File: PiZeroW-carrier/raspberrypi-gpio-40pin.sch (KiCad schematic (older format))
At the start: 8 parts, among them J1 40HAT, J2 CONN_02X02

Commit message: fix symbol for socket strip
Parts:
- removed J1: 40HAT, Socket_Strips:Socket_Strip_Straight_2x20, symbol OX40HAT
- added P?: CONN_02X20, Socket_Strips:Socket_Strip_Straight_2x20, symbol CONN_02X20
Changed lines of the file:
@@
 F 2 "project_footprints:NPTH_3mm_ID" H 5550 6000 60  0001 C CNN
 F 3 "" H 5550 6000 60  0001 C CNN
-F 4 "" H -12600 -4650 50  0001 C CNN "MFR"
-F 5 "" H -12600 -4650 50  0001 C CNN "MPN"
-F 6 "" H -12600 -4650 50  0001 C CNN "SPR"
-F 7 "" H -12600 -4650 50  0001 C CNN "SPN"
-F 8 "" H -12600 -4650 50  0001 C CNN "SPURL"
 	1    5650 6000
 	1    0    0    -1
@@
 F 8 "" H -12600 -4650 50  0001 C CNN "SPURL"
 	1    6700 6550
-	1    0    0    -1
-$EndComp
-$Comp
-L OX40HAT J1
-U 1 1 5A256561
-P 2600 2250
-F 0 "J1" H 2950 2350 50  0000 C CNN
-F 1 "40HAT" H 2300 2350 50  0000 C CNN
-F 2 "Socket_Strips:Socket_Strip_Straight_2x20" H 2600 2450 50  0000 C CNN
-F 3 "" H 1900 2250 50  0000 C CNN
-	1    2600 2250
 	1    0    0    -1
 $EndComp
@@
 Text Notes 5300 5700 0    118  ~ 24
 Mounting Holes
-Text Notes 1650 2000 0    118  ~ 24
+Text Notes 1600 1975 0    118  ~ 24
 40-Pin HAT Connector
-Text Label 800  4150 0    60   ~ 0
-GND
-Wire Wire Line
-	2000 4150 800  4150
-Text Label 800  3550 0    60   ~ 0
+Text Label 1150 4150 0    60   ~ 0
+GND
+Wire Wire Line
+	2350 4150 1150 4150
+Text Label 1150 3550 0    60   ~ 0
 SDA
 Wire Wire Line
-	2000 3550 800  3550
-Text Label 800  3450 0    60   ~ 0
-GND
-Wire Wire Line
-	2000 3450 800  3450
-Text Label 800  2650 0    60   ~ 0
-GND
-Wire Wire Line
-	2000 2650 800  2650
-Text Label 800  2250 0    60   ~ 0
+	2350 3550 1150 3550
+Text Label 1150 3450 0    60   ~ 0
+GND
+Wire Wire Line
+	2350 3450 1150 3450
+Text Label 1150 2650 0    60   ~ 0
+GND
+Wire Wire Line
+	2350 2650 1150 2650
+Text Label 1150 2250 0    60   ~ 0
 P3V3_HAT
 Wire Wire Line
-	2000 2250 800  2250
-Wire Wire Line
-	3200 2850 4400 2850
-Wire Wire Line
-	3200 3150 4400 3150
-Wire Wire Line
-	3200 3550 4400 3550
-Wire Wire Line
-	3200 3650 4400 3650
-Wire Wire Line
-	3200 3850 4400 3850
-Text Label 4400 2850 2    60   ~ 0
-GND
-Text Label 4400 3150 2    60   ~ 0
-GND
-Text Label 4400 3650 2    60   ~ 0
-GND
-Text Label 4400 3550 2    60   ~ 0
+	2350 2250 1150 2250
+Wire Wire Line
+	2850 2850 4050 2850
+Wire Wire Line
+	2850 3150 4050 3150
+Wire Wire Line
+	2850 3550 4050 3550
+Wire Wire Line
+	2850 3650 4050 3650
+Wire Wire Line
+	2850 3850 4050 3850
+Text Label 4050 2850 2    60   ~ 0
+GND
+Text Label 4050 3150 2    60   ~ 0
+GND
+Text Label 4050 3650 2    60   ~ 0
+GND
+Text Label 4050 3550 2    60   ~ 0
 SCL
-Text Label 4400 3850 2    60   ~ 0
-GND
-Text Label 4400 2450 2    60   ~ 0
-GND
-Wire Wire Line
-	3200 2450 4400 2450
-Wire Wire Line
-	3200 2350 4400 2350
-Wire Wire Line
-	3200 2250 4400 2250
+Text Label 4050 3850 2    60   ~ 0
+GND
+Text Label 4050 2450 2    60   ~ 0
+GND
+Wire Wire Line
+	2850 2450 4050 2450
+Wire Wire Line
+	2850 2350 4050 2350
+Wire Wire Line
+	2850 2250 4050 2250
 Text Notes 7150 4950 0    60   ~ 0
 HAT spec indicates to NEVER\npower the 3.3V pins on the Raspberry Pi \nfrom the HAT header. Only connect the 3.3V\npower from the Pi if the HAT does not have\n3.3V on board.\n\nIF you are designing a board that could\neither be powered by the Pi or from the HAT\nthe jumpers here can be used.\n\nIn most cases, either design the HAT \nto provide the 5V to the Pi and use the\nprotection circuit above OR power the\nHAT from the Pi and directly connect\nthe P3V3 and P5V to the P3V3_HAT and P5V_HAT\npins.
@@
 Text HLabel 5250 4700 0    60   Input ~ 0
 +5V
-Text HLabel 1145 2750 0    60   Input ~ 0
+Text HLabel 1495 2750 0    60   Input ~ 0
 LEDEnable
 Wire Wire Line
-	1145 2750 2000 2750
-NoConn ~ 2000 2350
-NoConn ~ 2000 2450
-NoConn ~ 2000 2550
-NoConn ~ 2000 2950
-NoConn ~ 2000 3050
-NoConn ~ 2000 3150
-NoConn ~ 2000 3250
-NoConn ~ 2000 3350
-NoConn ~ 2000 3650
-NoConn ~ 2000 3750
-NoConn ~ 2000 3850
-NoConn ~ 2000 3950
-NoConn ~ 2000 4050
-NoConn ~ 3200 4150
-NoConn ~ 3200 4050
-NoConn ~ 3200 3950
-NoConn ~ 3200 3750
-NoConn ~ 3200 3450
-NoConn ~ 3200 3350
-NoConn ~ 3200 3250
-NoConn ~ 3200 3050
-NoConn ~ 3200 2950
-NoConn ~ 3200 2750
-NoConn ~ 3200 2650
-NoConn ~ 3200 2550
-Text Label 4400 2350 2    60   ~ 0
+	1495 2750 2350 2750
+NoConn ~ 2350 2350
+NoConn ~ 2350 2450
+NoConn ~ 2350 2550
+NoConn ~ 2350 2950
+NoConn ~ 2350 3050
+NoConn ~ 2350 3150
+NoConn ~ 2350 3250
+NoConn ~ 2350 3350
+NoConn ~ 2350 3650
+NoConn ~ 2350 3750
+NoConn ~ 2350 3850
+NoConn ~ 2350 3950
+NoConn ~ 2350 4050
+NoConn ~ 2850 4150
+NoConn ~ 2850 4050
+NoConn ~ 2850 3950
+NoConn ~ 2850 3750
+NoConn ~ 2850 3450
+NoConn ~ 2850 3350
+NoConn ~ 2850 3250
+NoConn ~ 2850 3050
+NoConn ~ 2850 2950
+NoConn ~ 2850 2750
+NoConn ~ 2850 2650
+NoConn ~ 2850 2550
+Text Label 4050 2350 2    60   ~ 0
 P5V_HAT
-Text Label 4400 2250 2    60   ~ 0
+Text Label 4050 2250 2    60   ~ 0
 P5V_HAT
-Text HLabel 1140 2850 0    60   Input ~ 0
+Text HLabel 1490 2850 0    60   Input ~ 0
 PiDisable
 Wire Wire Line
-	1140 2850 2000 2850
+	1490 2850 2350 2850
+$Comp
+L CONN_02X20 P?
+U 1 1 5A26B31A
+P 2600 3200
+F 0 "P?" H 2600 4250 50  0000 C CNN
+F 1 "CONN_02X20" V 2600 3200 50  0000 C CNN
+F 2 "Socket_Strips:Socket_Strip_Straight_2x20" H 2625 2100 50  0000 C CNN
+F 3 "" H 2600 2250 50  0000 C CNN
+	1    2600 3200
+	1    0    0    -1
+$EndComp
 $EndSCHEMATC

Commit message: grab some more symbols and footprints from templates/raspberrrypi_hat
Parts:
- removed H1, H2, H3, H4: 3mm_Mounting_Hole, project_footprints:NPTH_3mm_ID, symbol 3mm_Mounting_Hole
- removed P?: CONN_02X20, Socket_Strips:Socket_Strip_Straight_2x20, symbol CONN_02X20
- added H? (x4): Hole_3mm_PTH, symbol Hole_3mm_PTH
- added J?: PI40HAT, OX40_Module_Header, symbol PI40HAT
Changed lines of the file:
@@
 LIBS:valves
 LIBS:ba06cc0wfp-e2ct
+LIBS:raspberrypi_hat
+LIBS:PiZeroW-carrier-cache
 EELAYER 25 0
 EELAYER END
@@
 $EndDescr
 $Comp
-L 3mm_Mounting_Hole H1
-U 1 1 5A25655D
-P 5650 6000
-F 0 "H1" H 5500 6100 60  0000 C CNN
-F 1 "3mm_Mounting_Hole" H 5650 5850 60  0000 C CNN
-F 2 "project_footprints:NPTH_3mm_ID" H 5550 6000 60  0001 C CNN
-F 3 "" H 5550 6000 60  0001 C CNN
-	1    5650 6000
-	1    0    0    -1
-$EndComp
-$Comp
-L 3mm_Mounting_Hole H3
-U 1 1 5A25655E
-P 6650 6000
-F 0 "H3" H 6500 6100 60  0000 C CNN
-F 1 "3mm_Mounting_Hole" H 6650 5850 60  0000 C CNN
-F 2 "project_footprints:NPTH_3mm_ID" H 6550 6000 60  0001 C CNN
-F 3 "" H 6550 6000 60  0001 C CNN
-F 4 "" H -12600 -4650 50  0001 C CNN "MFR"
-F 5 "" H -12600 -4650 50  0001 C CNN "MPN"
-F 6 "" H -12600 -4650 50  0001 C CNN "SPR"
-F 7 "" H -12600 -4650 50  0001 C CNN "SPN"
-F 8 "" H -12600 -4650 50  0001 C CNN "SPURL"
-	1    6650 6000
-	1    0    0    -1
-$EndComp
-$Comp
-L 3mm_Mounting_Hole H2
-U 1 1 5A25655F
-P 5650 6550
-F 0 "H2" H 5500 6650 60  0000 C CNN
-F 1 "3mm_Mounting_Hole" H 5650 6400 60  0000 C CNN
-F 2 "project_footprints:NPTH_3mm_ID" H 5550 6550 60  0001 C CNN
-F 3 "" H 5550 6550 60  0001 C CNN
-F 4 "" H -12600 -4650 50  0001 C CNN "MFR"
-F 5 "" H -12600 -4650 50  0001 C CNN "MPN"
-F 6 "" H -12600 -4650 50  0001 C CNN "SPR"
-F 7 "" H -12600 -4650 50  0001 C CNN "SPN"
-F 8 "" H -12600 -4650 50  0001 C CNN "SPURL"
-	1    5650 6550
-	1    0    0    -1
-$EndComp
-$Comp
-L 3mm_Mounting_Hole H4
-U 1 1 5A256560
-P 6700 6550
-F 0 "H4" H 6550 6650 60  0000 C CNN
-F 1 "3mm_Mounting_Hole" H 6700 6400 60  0000 C CNN
-F 2 "project_footprints:NPTH_3mm_ID" H 6600 6550 60  0001 C CNN
-F 3 "" H 6600 6550 60  0001 C CNN
-F 4 "" H -12600 -4650 50  0001 C CNN "MFR"
-F 5 "" H -12600 -4650 50  0001 C CNN "MPN"
-F 6 "" H -12600 -4650 50  0001 C CNN "SPR"
-F 7 "" H -12600 -4650 50  0001 C CNN "SPN"
-F 8 "" H -12600 -4650 50  0001 C CNN "SPURL"
-	1    6700 6550
-	1    0    0    -1
-$EndComp
-$Comp
 L CONN_02X02 J2
 U 1 1 5A256562
@@
 Text Notes 5300 5700 0    118  ~ 24
 Mounting Holes
-Text Notes 1600 1975 0    118  ~ 24
+Text Notes 2045 1875 0    118  ~ 24
 40-Pin HAT Connector
 Text Label 1150 4150 0    60   ~ 0
@@
 	2350 2250 1150 2250
 Wire Wire Line
-	2850 2850 4050 2850
-Wire Wire Line
-	2850 3150 4050 3150
-Wire Wire Line
-	2850 3550 4050 3550
-Wire Wire Line
-	2850 3650 4050 3650
-Wire Wire Line
-	2850 3850 4050 3850
-Text Label 4050 2850 2    60   ~ 0
-GND
-Text Label 4050 3150 2    60   ~ 0
-GND
-Text Label 4050 3650 2    60   ~ 0
-GND
-Text Label 4050 3550 2    60   ~ 0
+	3550 2850 4750 2850
+Wire Wire Line
+	3550 3150 4750 3150
+Wire Wire Line
+	3550 3550 4750 3550
+Wire Wire Line
+	3550 3650 4750 3650
+Wire Wire Line
+	3550 3850 4750 3850
+Text Label 4750 2850 2    60   ~ 0
+GND
+Text Label 4750 3150 2    60   ~ 0
+GND
+Text Label 4750 3650 2    60   ~ 0
+GND
+Text Label 4750 3550 2    60   ~ 0
 SCL
-Text Label 4050 3850 2    60   ~ 0
-GND
-Text Label 4050 2450 2    60   ~ 0
-GND
-Wire Wire Line
-	2850 2450 4050 2450
-Wire Wire Line
-	2850 2350 4050 2350
-Wire Wire Line
-	2850 2250 4050 2250
+Text Label 4750 3850 2    60   ~ 0
+GND
+Text Label 4750 2450 2    60   ~ 0
+GND
+Wire Wire Line
+	3550 2450 4750 2450
+Wire Wire Line
+	3550 2350 4750 2350
+Wire Wire Line
+	3550 2250 4750 2250
 Text Notes 7150 4950 0    60   ~ 0
 HAT spec indicates to NEVER\npower the 3.3V pins on the Raspberry Pi \nfrom the HAT header. Only connect the 3.3V\npower from the Pi if the HAT does not have\n3.3V on board.\n\nIF you are designing a board that could\neither be powered by the Pi or from the HAT\nthe jumpers here can be used.\n\nIn most cases, either design the HAT \nto provide the 5V to the Pi and use the\nprotection circuit above OR power the\nHAT from the Pi and directly connect\nthe P3V3 and P5V to the P3V3_HAT and P5V_HAT\npins.
@@
 NoConn ~ 2350 3950
 NoConn ~ 2350 4050
-NoConn ~ 2850 4150
-NoConn ~ 2850 4050
-NoConn ~ 2850 3950
-NoConn ~ 2850 3750
-NoConn ~ 2850 3450
-NoConn ~ 2850 3350
-NoConn ~ 2850 3250
-NoConn ~ 2850 3050
-NoConn ~ 2850 2950
-NoConn ~ 2850 2750
-NoConn ~ 2850 2650
-NoConn ~ 2850 2550
-Text Label 4050 2350 2    60   ~ 0
+NoConn ~ 3550 4150
+NoConn ~ 3550 4050
+NoConn ~ 3550 3950
+NoConn ~ 3550 3750
+NoConn ~ 3550 3450
+NoConn ~ 3550 3350
+NoConn ~ 3550 3250
+NoConn ~ 3550 3050
+NoConn ~ 3550 2950
+NoConn ~ 3550 2750
+NoConn ~ 3550 2650
+NoConn ~ 3550 2550
+Text Label 4750 2350 2    60   ~ 0
 P5V_HAT
-Text Label 4050 2250 2    60   ~ 0
+Text Label 4750 2250 2    60   ~ 0
 P5V_HAT
 Text HLabel 1490 2850 0    60   Input ~ 0
@@
 	1490 2850 2350 2850
 $Comp
-L CONN_02X20 P?
-U 1 1 5A26B31A
-P 2600 3200
-F 0 "P?" H 2600 4250 50  0000 C CNN
-F 1 "CONN_02X20" V 2600 3200 50  0000 C CNN
-F 2 "Socket_Strips:Socket_Strip_Straight_2x20" H 2625 2100 50  0000 C CNN
-F 3 "" H 2600 2250 50  0000 C CNN
-	1    2600 3200
-	1    0    0    -1
-$EndComp
+L Hole_3mm_PTH H?
+U 1 1 5A26C7D1
+P 5540 5960
+F 0 "H?" H 5390 6060 60  0000 C CNN
+F 1 "Hole_3mm_PTH" H 5540 5810 60  0000 C CNN
+F 2 "" H 5440 5960 60  0001 C CNN
+F 3 "" H 5440 5960 60  0001 C CNN
+	1    5540 5960
+	1    0    0    -1
+$EndComp
+$Comp
+L Hole_3mm_PTH H?
+U 1 1 5A26C958
+P 5540 6440
+F 0 "H?" H 5390 6540 60  0000 C CNN
+F 1 "Hole_3mm_PTH" H 5540 6290 60  0000 C CNN
+F 2 "" H 5440 6440 60  0001 C CNN
+F 3 "" H 5440 6440 60  0001 C CNN
+	1    5540 6440
+	1    0    0    -1
+$EndComp
+$Comp
+L Hole_3mm_PTH H?
+U 1 1 5A26C9EB
+P 6540 5950
+F 0 "H?" H 6390 6050 60  0000 C CNN
+F 1 "Hole_3mm_PTH" H 6540 5800 60  0000 C CNN
+F 2 "" H 6440 5950 60  0001 C CNN
+F 3 "" H 6440 5950 60  0001 C CNN
+	1    6540 5950
+	1    0    0    -1
+$EndComp
+$Comp
+L Hole_3mm_PTH H?
+U 1 1 5A26C9F1
+P 6540 6430
+F 0 "H?" H 6390 6530 60  0000 C CNN
+F 1 "Hole_3mm_PTH" H 6540 6280 60  0000 C CNN
+F 2 "" H 6440 6430 60  0001 C CNN
+F 3 "" H 6440 6430 60  0001 C CNN
+	1    6540 6430
+	1    0    0    -1
+$EndComp
+$Comp
+L PI40HAT J?
+U 1 1 5A26CB8A
+P 2950 2250
+F 0 "J?" H 3300 2350 50  0000 C CNN
+F 1 "PI40HAT" H 2650 2350 50  0000 C CNN
+F 2 "OX40_Module_Header" H 2950 2450 50  0000 C CNN
+F 3 "" H 2250 2250 50  0000 C CNN
+	1    2950 2250
+	1    0    0    -1
+$EndComp

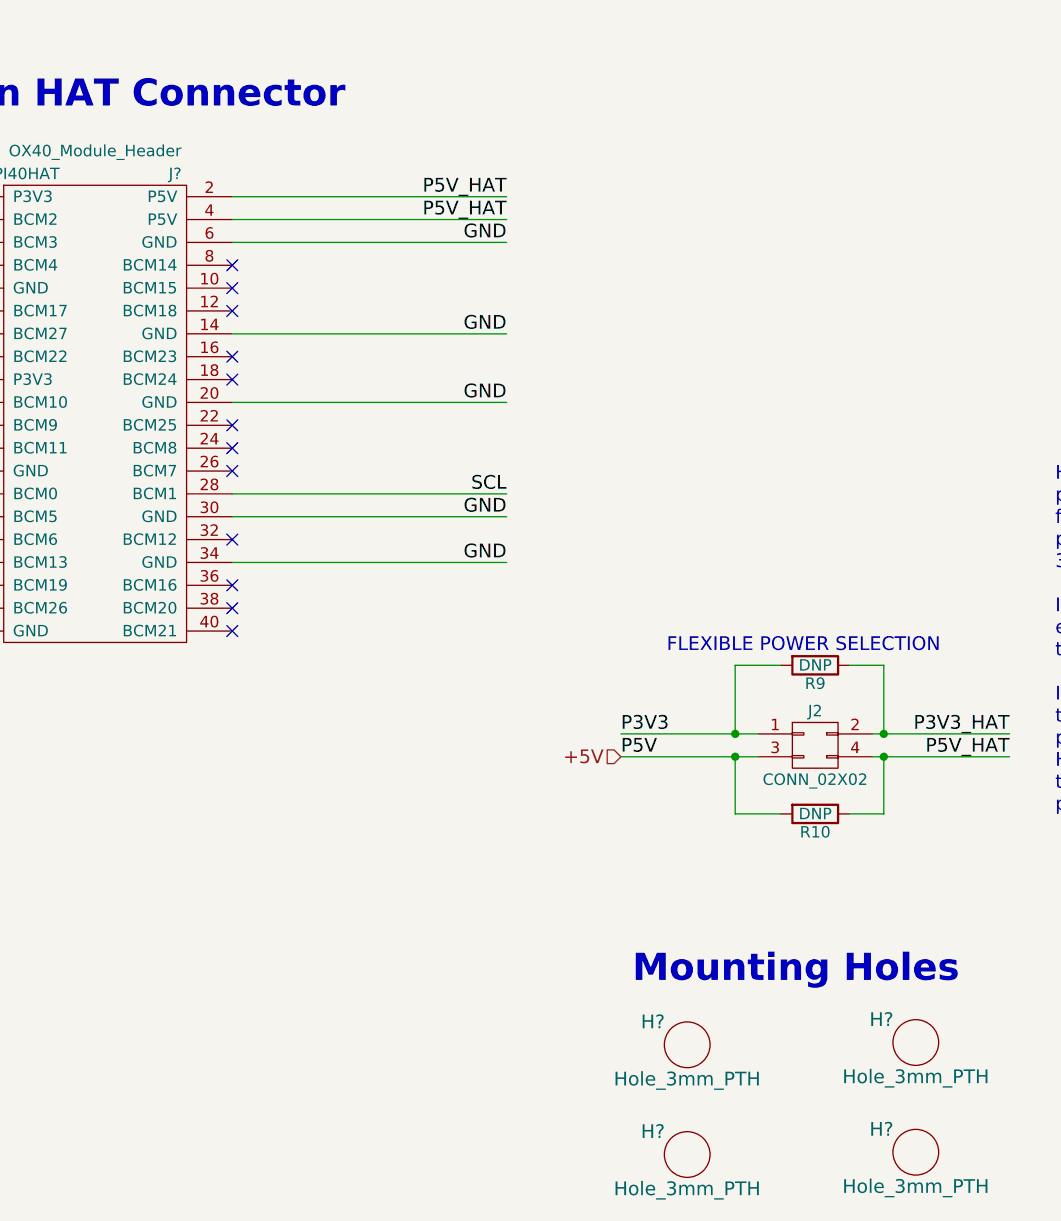
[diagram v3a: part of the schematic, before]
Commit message: assign component footprints
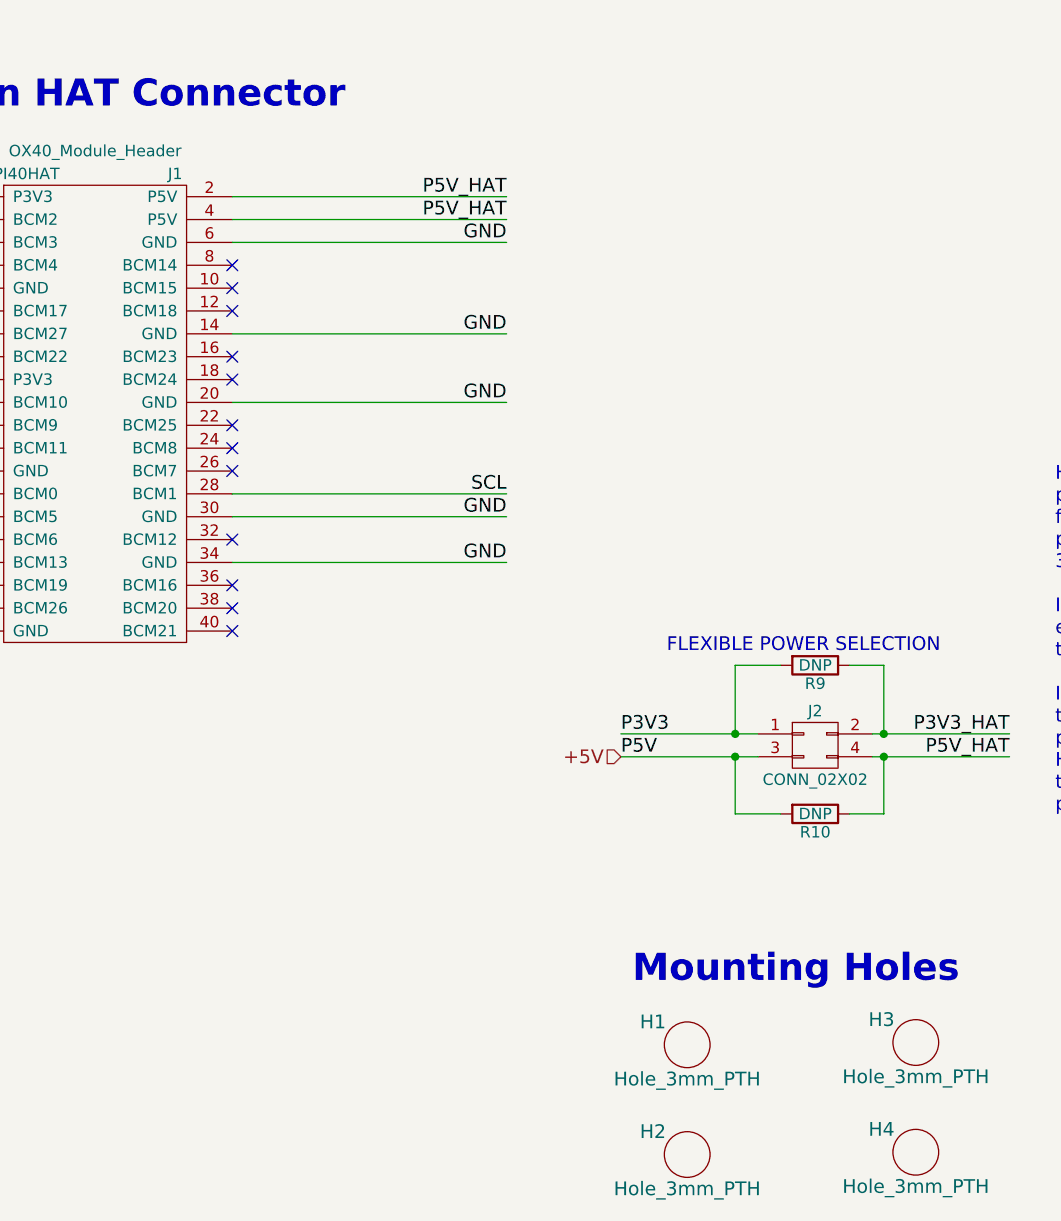
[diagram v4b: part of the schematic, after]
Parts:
- H1, H2, H3, H4: renamed from H?; footprint (none) -> lib_fp:NPTH_3mm_ID
- gave numbers to parts that had none: 1
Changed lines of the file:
@@
 	1490 2850 2350 2850
 $Comp
-L Hole_3mm_PTH H?
+L Hole_3mm_PTH H1
 U 1 1 5A26C7D1
 P 5540 5960
-F 0 "H?" H 5390 6060 60  0000 C CNN
+F 0 "H1" H 5390 6060 60  0000 C CNN
 F 1 "Hole_3mm_PTH" H 5540 5810 60  0000 C CNN
-F 2 "" H 5440 5960 60  0001 C CNN
+F 2 "lib_fp:NPTH_3mm_ID" H 5440 5960 60  0001 C CNN
 F 3 "" H 5440 5960 60  0001 C CNN
 	1    5540 5960
@@
 $EndComp
 $Comp
-L Hole_3mm_PTH H?
+L Hole_3mm_PTH H2
 U 1 1 5A26C958
 P 5540 6440
-F 0 "H?" H 5390 6540 60  0000 C CNN
+F 0 "H2" H 5390 6540 60  0000 C CNN
 F 1 "Hole_3mm_PTH" H 5540 6290 60  0000 C CNN
-F 2 "" H 5440 6440 60  0001 C CNN
+F 2 "lib_fp:NPTH_3mm_ID" H 5440 6440 60  0001 C CNN
 F 3 "" H 5440 6440 60  0001 C CNN
 	1    5540 6440
@@
 $EndComp
 $Comp
-L Hole_3mm_PTH H?
+L Hole_3mm_PTH H3
 U 1 1 5A26C9EB
 P 6540 5950
-F 0 "H?" H 6390 6050 60  0000 C CNN
+F 0 "H3" H 6390 6050 60  0000 C CNN
 F 1 "Hole_3mm_PTH" H 6540 5800 60  0000 C CNN
-F 2 "" H 6440 5950 60  0001 C CNN
+F 2 "lib_fp:NPTH_3mm_ID" H 6440 5950 60  0001 C CNN
 F 3 "" H 6440 5950 60  0001 C CNN
 	1    6540 5950
@@
 $EndComp
 $Comp
-L Hole_3mm_PTH H?
+L Hole_3mm_PTH H4
 U 1 1 5A26C9F1
 P 6540 6430
-F 0 "H?" H 6390 6530 60  0000 C CNN
+F 0 "H4" H 6390 6530 60  0000 C CNN
 F 1 "Hole_3mm_PTH" H 6540 6280 60  0000 C CNN
-F 2 "" H 6440 6430 60  0001 C CNN
+F 2 "lib_fp:NPTH_3mm_ID" H 6440 6430 60  0001 C CNN
 F 3 "" H 6440 6430 60  0001 C CNN
 	1    6540 6430
@@
 $EndComp
 $Comp
-L PI40HAT J?
+L PI40HAT J1
 U 1 1 5A26CB8A
 P 2950 2250
-F 0 "J?" H 3300 2350 50  0000 C CNN
+F 0 "J1" H 3300 2350 50  0000 C CNN
 F 1 "PI40HAT" H 2650 2350 50  0000 C CNN
 F 2 "OX40_Module_Header" H 2950 2450 50  0000 C CNN

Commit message: netlist update and read into pcb
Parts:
- J1: footprint OX40_Module_Header -> Pin_Headers:Pin_Header_Straight_2x20_Pitch2.54mm
- J2: footprint Pin_Headers:Pin_Header_Straight_2x02 -> Pin_Headers:Pin_Header_Straight_2x02_Pitch2.54mm
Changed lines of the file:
@@
 EESchema Schematic File Version 2
+LIBS:PiZeroW-carrier-rescue
 LIBS:power
 LIBS:device
@@
 F 0 "J2" H 6100 4800 50  0000 C CNN
 F 1 "CONN_02X02" H 6100 4500 50  0000 C CNN
-F 2 "Pin_Headers:Pin_Header_Straight_2x02" H 6100 3450 50  0001 C CNN
+F 2 "Pin_Headers:Pin_Header_Straight_2x02_Pitch2.54mm" H 6100 3450 50  0001 C CNN
 F 3 "" H 6100 3450 50  0000 C CNN
 	1    6100 4650
@@
 F 0 "J1" H 3300 2350 50  0000 C CNN
 F 1 "PI40HAT" H 2650 2350 50  0000 C CNN
-F 2 "OX40_Module_Header" H 2950 2450 50  0000 C CNN
+F 2 "Pin_Headers:Pin_Header_Straight_2x20_Pitch2.54mm" H 2950 2450 50  0000 C CNN
 F 3 "" H 2250 2250 50  0000 C CNN
 	1    2950 2250
